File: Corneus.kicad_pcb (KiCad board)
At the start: 2 copper layers, 262 x 112 mm, 145 parts, among them J1 USB_B_Micro, Q1 Q_NPN_BCE, SW1 SW_Push, U1 ATmega32U4-AU, U2 PRTR5V0U2X, Y1 16MHz

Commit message: routed switch rows and columns
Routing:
- net ROW2: track 0.00 -> 264.6 mm, vias 0 -> 2
- net ROW1: track 0.00 -> 257.2 mm, vias 0 -> 2
- net ROW0: track 20.4 -> 247.7 mm, vias 0 -> 2
- net COL6: track 0.00 -> 77.0 mm
- net COL5: track 0.00 -> 71.8 mm
- net COL7: track 0.00 -> 70.0 mm
- net COL8: track 0.00 -> 69.8 mm
- net COL3: track 0.00 -> 69.8 mm
- net COL4: track 0.00 -> 67.0 mm
- net COL2: track 0.00 -> 40.8 mm
- net COL9: track 0.00 -> 40.8 mm
- net COL10: track 0.00 -> 40.8 mm
- net COL1: track 0.00 -> 40.8 mm
- net COL11: track 0.00 -> 40.8 mm
- net LEDGND: track 0.00 -> 20.6 mm, vias 0 -> 2
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
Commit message: routed LEDGND and the missed bottom switch row
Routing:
- net LEDGND: track 20.6 -> 1026.9 mm, vias 2 -> 8
- net ROW3: track 0.00 -> 141.2 mm
- net Net-(MX3-Pad4): track 0.00 -> 8.81 mm, vias 0 -> 1

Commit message: routed more LED stuff
-routed LED +5V
-removed unnecessary traces between hands (just because I relied on LED rows in the handwire doesn't mean I have to on this PCB)
-routed all LEDs to their respective resistors
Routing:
- net +5V: track 189.7 -> 1099.2 mm, vias 0 -> 27
- net LEDGND: track 1026.9 -> 952.9 mm
- net Net-(MX41-Pad4): track 0.00 -> 12.0 mm, vias 0 -> 1
- net Net-(MX15-Pad4): track 0.00 -> 11.2 mm, vias 0 -> 1
- net Net-(MX28-Pad4): track 0.00 -> 10.7 mm, vias 0 -> 1
- net Net-(MX27-Pad4): track 0.00 -> 10.6 mm, vias 0 -> 1
- net Net-(MX40-Pad4): track 0.00 -> 10.4 mm, vias 0 -> 1
- net Net-(MX42-Pad4): track 0.00 -> 10.4 mm, vias 0 -> 1
- net Net-(MX16-Pad4): track 0.00 -> 10.3 mm, vias 0 -> 1
- net Net-(MX13-Pad4): track 0.00 -> 9.79 mm, vias 0 -> 1
- net Net-(MX6-Pad4): track 0.00 -> 9.64 mm, vias 0 -> 1
- net Net-(MX29-Pad4): track 0.00 -> 9.54 mm, vias 0 -> 1
- net Net-(MX34-Pad4): track 0.00 -> 9.44 mm, vias 0 -> 1
- net Net-(MX24-Pad4): track 0.00 -> 9.08 mm, vias 0 -> 1
- net Net-(MX38-Pad4): track 0.00 -> 9.07 mm
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
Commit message: replaced MOSFET footprint, started routing right hand columns
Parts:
- Q1: footprint Package_TO_SOT_SMD:SOT-223 -> digikey-footprints:Trans_SOT-223-4
- turned Q1 to 270 degrees
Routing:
- net COL11: track 40.8 -> 195.0 mm, vias 0 -> 1
- net COL10: track 40.8 -> 182.2 mm, vias 0 -> 1
- net COL9: track 40.8 -> 154.9 mm, vias 0 -> 1
- net COL8: track 69.8 -> 153.4 mm, vias 0 -> 1
- net COL7: track 70.0 -> 132.7 mm, vias 0 -> 1
- net LEDGND: track 952.9 -> 955.6 mm

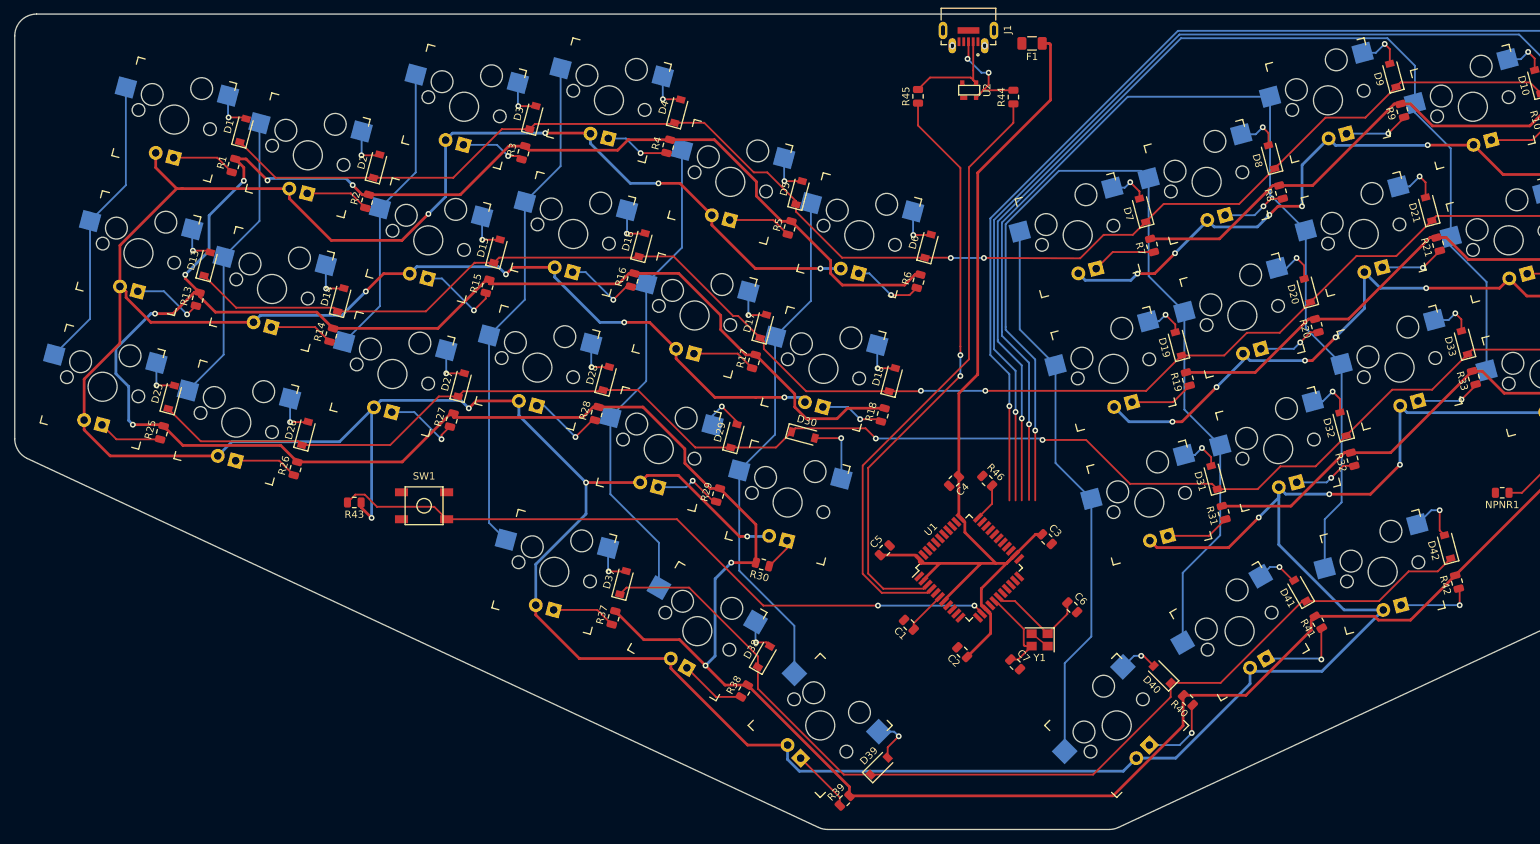
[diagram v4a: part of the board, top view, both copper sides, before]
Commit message: routed rows and columns
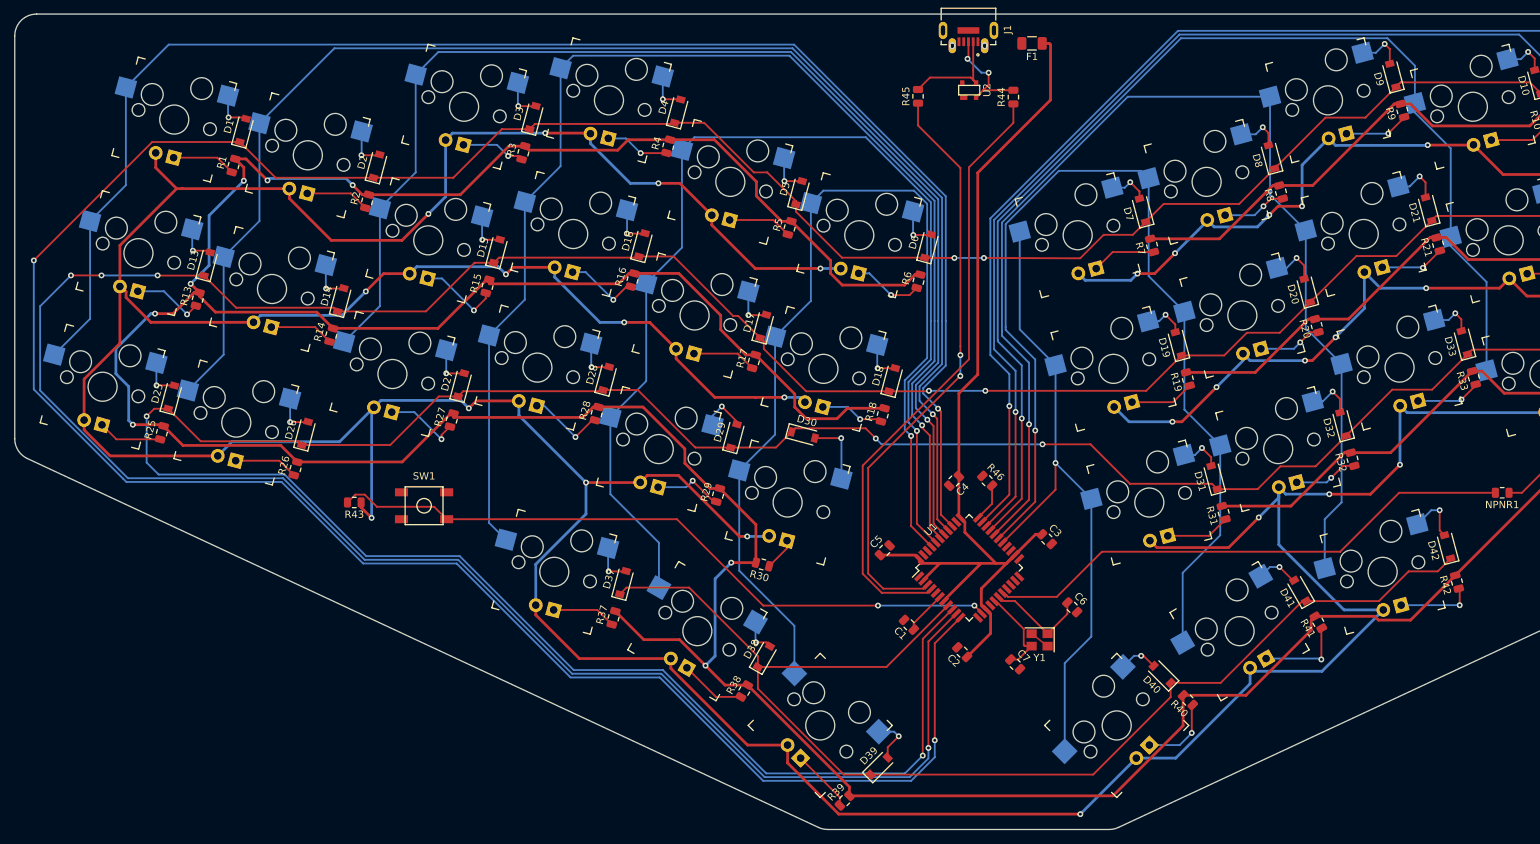
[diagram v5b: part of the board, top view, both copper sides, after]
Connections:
- U1 pad 10: Net-(U1-Pad10) -> ROW1
- U1 pad 11: Net-(U1-Pad11) -> ROW0
- U1 pad 18: Net-(U1-Pad18) -> LEDPWM
- U1 pad 27: Net-(U1-Pad27) -> COL6
- U1 pad 28: Net-(U1-Pad28) -> COL7
- U1 pad 29: Net-(U1-Pad29) -> COL8
- U1 pad 30: Net-(U1-Pad30) -> COL9
- U1 pad 31: Net-(U1-Pad31) -> COL10
- U1 pad 32: Net-(U1-Pad32) -> COL11
- U1 pad 36: Net-(U1-Pad36) -> COL0
- U1 pad 37: Net-(U1-Pad37) -> COL1
- U1 pad 38: Net-(U1-Pad38) -> COL2
- U1 pad 39: Net-(U1-Pad39) -> COL3
- U1 pad 40: Net-(U1-Pad40) -> COL4
- U1 pad 41: Net-(U1-Pad41) -> COL5
- U1 pad 8: Net-(U1-Pad8) -> ROW3
- U1 pad 9: Net-(U1-Pad9) -> ROW2
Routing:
- net ROW0: track 247.6 -> 468.4 mm, vias 2 -> 4
- net ROW1: track 257.2 -> 459.6 mm, vias 2 -> 6
- net COL0: track 40.8 -> 212.7 mm, vias 0 -> 1
- net ROW2: track 264.6 -> 421.4 mm, vias 2 -> 4
- net COL1: track 40.8 -> 195.9 mm, vias 0 -> 1
- net COL2: track 40.8 -> 171.1 mm, vias 0 -> 1
- net COL3: track 69.8 -> 179.4 mm, vias 0 -> 1
- net COL4: track 67.0 -> 155.1 mm, vias 0 -> 1
- net LEDPWM: track 0.00 -> 73.8 mm
- net COL5: track 71.8 -> 139.1 mm, vias 0 -> 1
- net ROW3: track 141.2 -> 170.8 mm
- net COL6: track 77.0 -> 90.9 mm, vias 0 -> 1
- net COL7: track 132.7 -> 140.0 mm
- net COL8: track 153.4 -> 160.1 mm
- net COL9: track 154.9 -> 160.8 mm
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
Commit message: added mounting holes
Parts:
- added REF**: NPTH_2.2_4, Choco617_parts:NPTH_2.2_4, F.Cu at (169.4, 130.5)
- added REF**: NPTH_2.2_4, Choco617_parts:NPTH_2.2_4, F.Cu at (120.4, 58.0)
- added REF**: NPTH_2.2_4, Choco617_parts:NPTH_2.2_4, F.Cu at (127.4, 130.5)
- added REF**: NPTH_2.2_4, Choco617_parts:NPTH_2.2_4, F.Cu at (210.4, 111.0)
- added REF**: NPTH_2.2_4, Choco617_parts:NPTH_2.2_4, F.Cu at (86.4, 111.0)
- added REF**: NPTH_2.2_4, Choco617_parts:NPTH_2.2_4, F.Cu at (271.4, 58.0)
- added REF**: NPTH_2.2_4, Choco617_parts:NPTH_2.2_4, F.Cu at (25.4, 58.0)
- added REF**: NPTH_2.2_4, Choco617_parts:NPTH_2.2_4, F.Cu at (231.4, 58.0)
- added REF**: NPTH_2.2_4, Choco617_parts:NPTH_2.2_4, F.Cu at (65.4, 58.0)
- added REF**: NPTH_2.2_4, Choco617_parts:NPTH_2.2_4, F.Cu at (176.4, 58.0)
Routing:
- net Net-(R43-Pad2): track 94.6 -> 97.2 mm
- net +5V: track 1104.4 -> 1102.9 mm
- net COL10: track 187.4 -> 188.6 mm

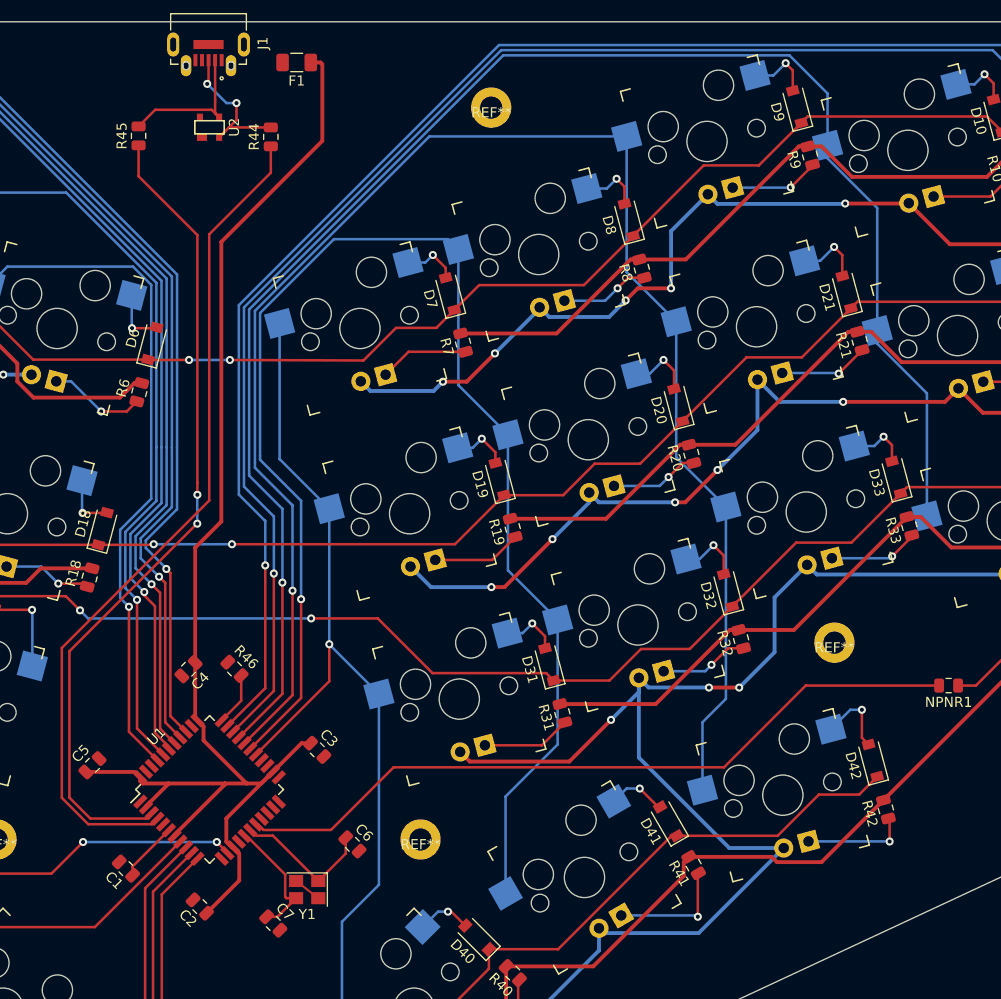
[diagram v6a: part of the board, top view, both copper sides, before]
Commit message: routed decoupling capacitors 5V
-also swapped 10uF cap with one of the 0.1uF ones to put the 10 in the correct place
-about to rotate the whole MCU region 180 degrees to correct a USB routing sin, this is going to involve rerouting all the row/column connections to the MCU but probably result in tidier traces overall
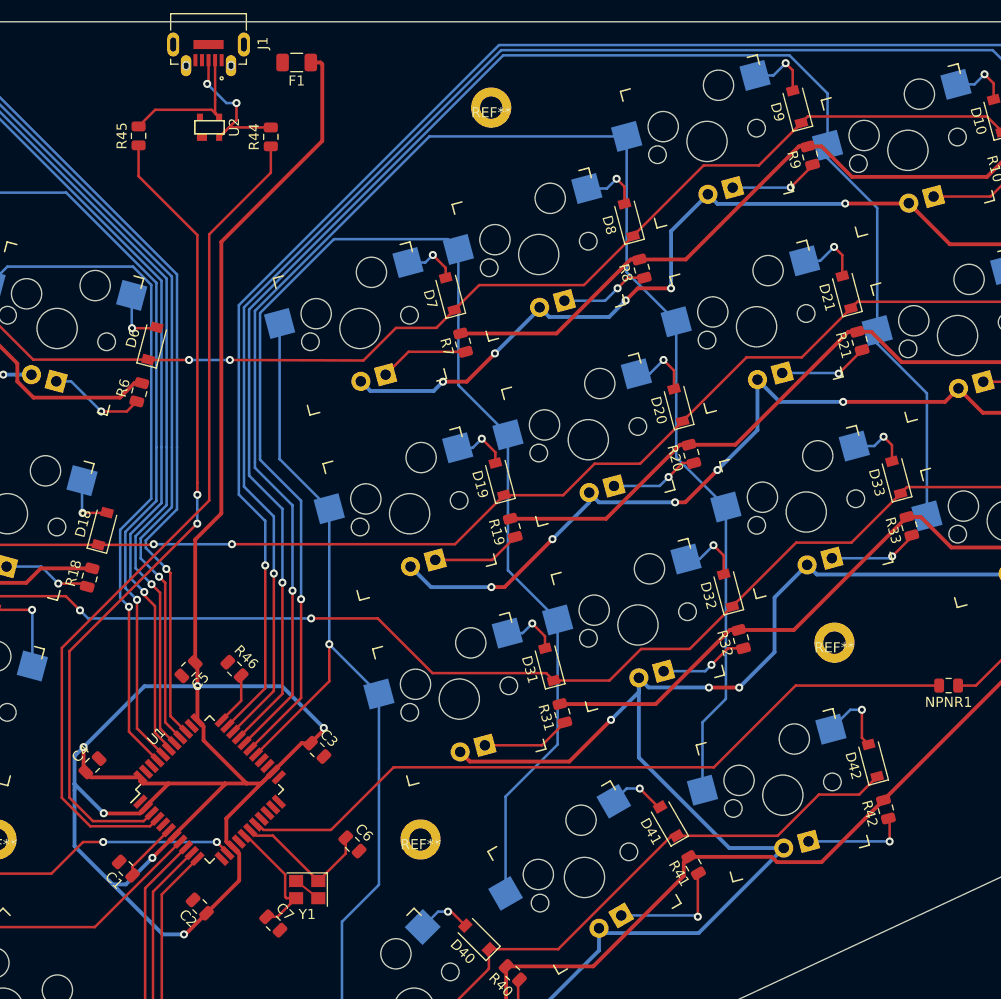
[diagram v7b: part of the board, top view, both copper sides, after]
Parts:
- moved C4 13.5 mm to (136.9, 123.1), turned to 45 degrees
- moved C5 13.5 mm to (146.4, 113.6), turned to 225 degrees
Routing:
- net +5V: track 1102.9 -> 1180.5 mm, vias 28 -> 34

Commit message: rotated MCU region and routed rows
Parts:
- moved R43 83.1 mm to (144.9, 97.1), turned to 270 degrees
- moved SW1 70.1 mm to (143.0, 107.1), turned to 270 degrees
- moved C6 29.0 mm to (134.6, 123.6), turned to 135 degrees
- moved R46 27.8 mm to (146.3, 141.0), turned to 135 degrees
- moved C7 26.2 mm to (142.5, 115.8), turned to 135 degrees
- moved Y1 25.1 mm to (139.1, 119.1), turned to 0 degrees
- moved REF** 24.2 mm to (276.4, 81.7)
- moved REF** 24.2 mm to (20.4, 81.7)
- moved C3 24.0 mm to (138.1, 133.0), turned to 135 degrees
- moved C4 23.6 mm to (157.8, 134.1), turned to 225 degrees
- moved C1 19.8 mm to (151.9, 117.4)
- moved F1 15.9 mm to (142.8, 60.4), turned to 90 degrees
- moved R45 9.48 mm to (149.4, 66.0)
- moved R44 8.80 mm to (147.4, 66.0)
- moved C2 5.00 mm to (150.8, 141.0), turned to 45 degrees
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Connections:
- U1 pad 18: LEDPWM -> Net-(U1-Pad18)
- U1 pad 27: COL6 -> Net-(U1-Pad27)
- U1 pad 28: COL7 -> Net-(U1-Pad28)
- U1 pad 29: COL8 -> Net-(U1-Pad29)
- U1 pad 30: COL9 -> Net-(U1-Pad30)
- U1 pad 31: COL10 -> Net-(U1-Pad31)
- U1 pad 32: COL11 -> Net-(U1-Pad32)
- U1 pad 36: COL0 -> Net-(U1-Pad36)
- U1 pad 37: COL1 -> Net-(U1-Pad37)
- U1 pad 38: COL2 -> Net-(U1-Pad38)
- U1 pad 39: COL3 -> Net-(U1-Pad39)
- U1 pad 40: COL4 -> Net-(U1-Pad40)
- U1 pad 41: COL5 -> Net-(U1-Pad41)
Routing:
- net COL0: track 212.7 -> 40.8 mm, vias 1 -> 0
- net ROW1: track 459.6 -> 289.0 mm, vias 6 -> 4
- net ROW0: track 468.4 -> 298.0 mm
- net COL11: track 199.5 -> 40.8 mm, vias 1 -> 0
- net COL1: track 195.9 -> 40.8 mm, vias 1 -> 0
- net COL10: track 188.6 -> 40.8 mm, vias 1 -> 0
- net COL2: track 171.1 -> 40.8 mm, vias 1 -> 0
- net ROW2: track 421.4 -> 300.4 mm, vias 4 -> 2
- net COL9: track 160.8 -> 40.8 mm, vias 1 -> 0
- net COL3: track 179.4 -> 69.8 mm, vias 1 -> 0
- net COL8: track 160.1 -> 69.8 mm, vias 1 -> 0
- net COL4: track 155.1 -> 67.0 mm, vias 1 -> 0
- net LEDPWM: track 73.8 -> 0.00 mm
- net COL7: track 140.0 -> 70.0 mm, vias 1 -> 0
- net COL5: track 139.1 -> 71.8 mm, vias 1 -> 0
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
